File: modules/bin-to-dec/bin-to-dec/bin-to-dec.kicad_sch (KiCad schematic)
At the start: 1 part, among them J1 Conn_02x26_Odd_Even

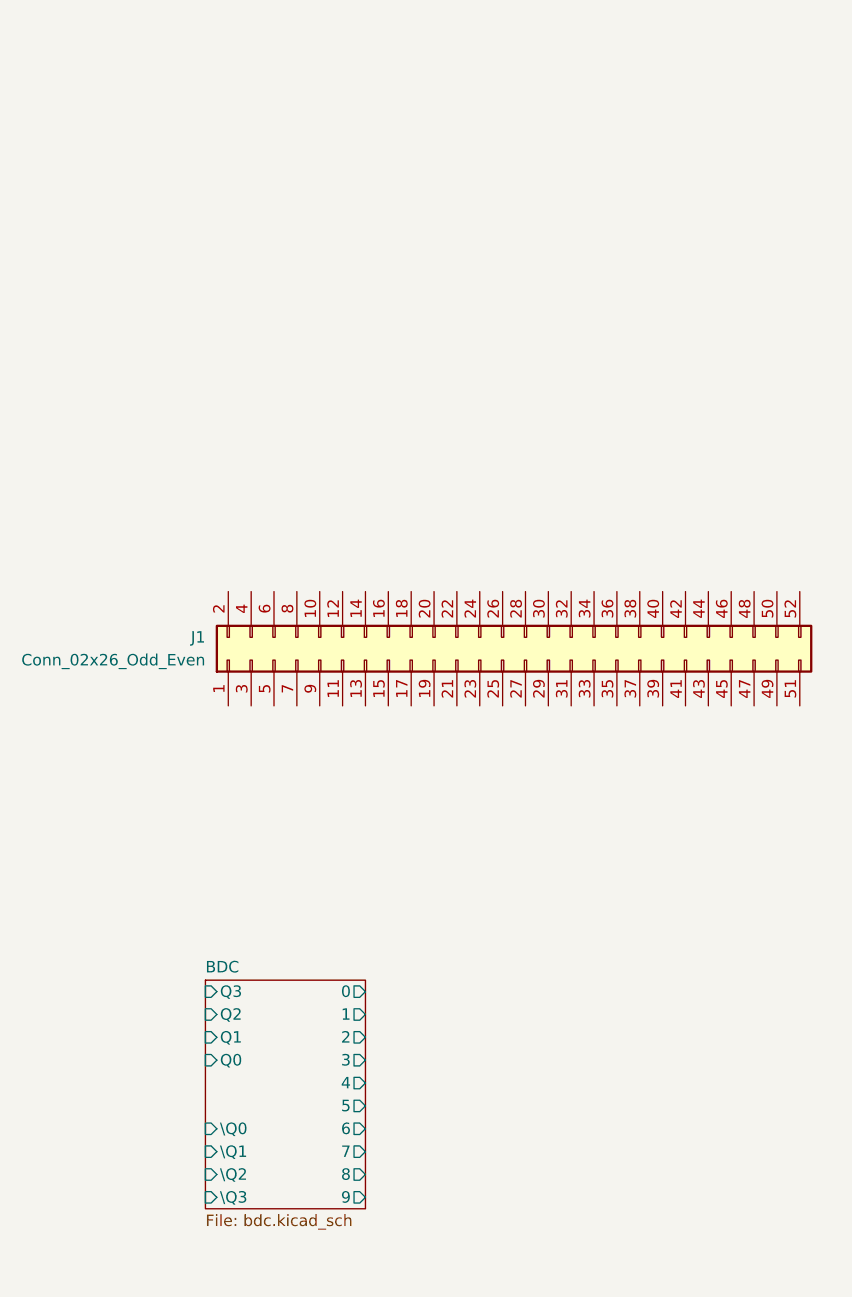
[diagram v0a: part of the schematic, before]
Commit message: routed on bdc
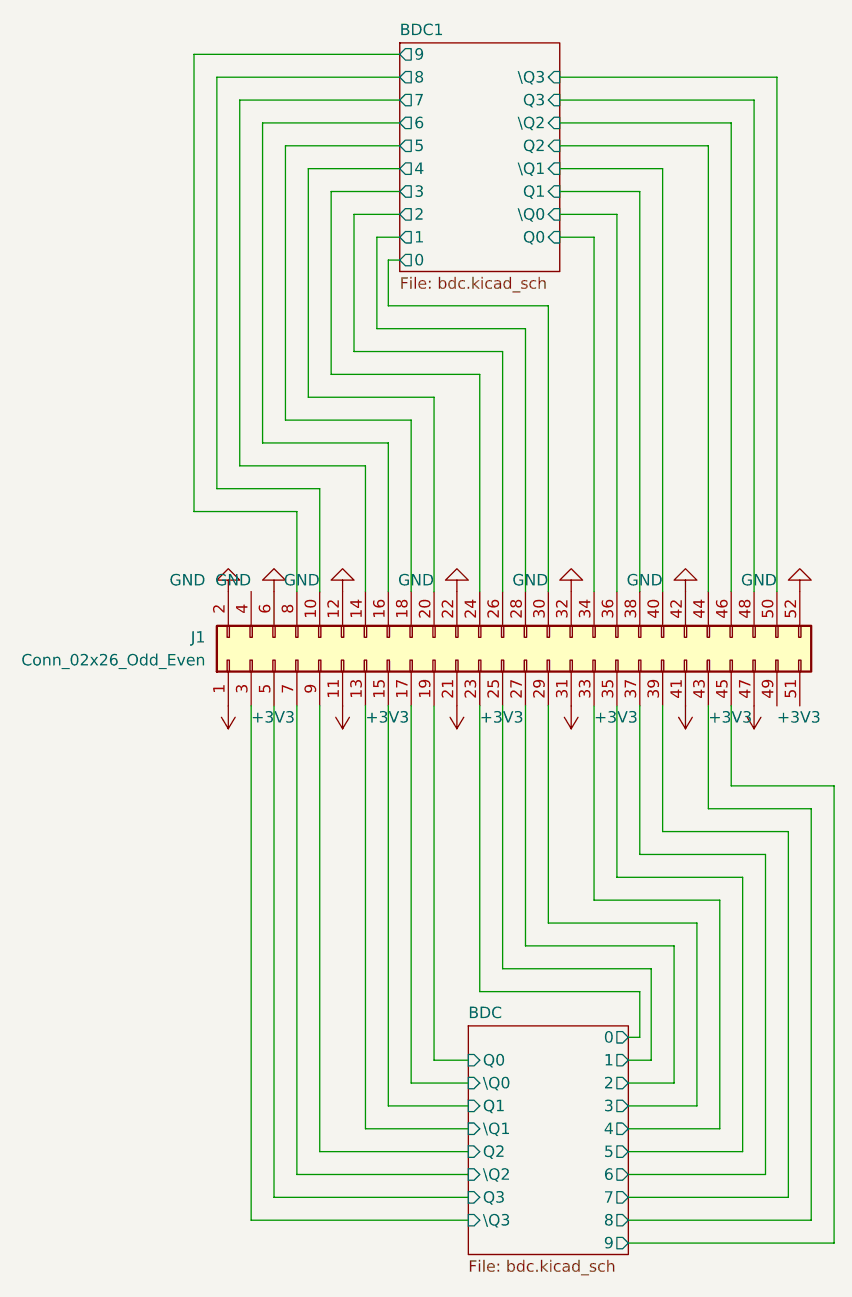
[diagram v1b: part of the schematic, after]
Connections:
- net BDC/0: now also J1.23 (Pin_23)
- net BDC/1: now also J1.25 (Pin_25)
- net BDC/2: now also J1.27 (Pin_27)
- net BDC/3: now also J1.29 (Pin_29)
- net BDC/4: now also J1.33 (Pin_33)
- net BDC/5: now also J1.35 (Pin_35)
- net BDC/6: now also J1.37 (Pin_37)
- net BDC/7: now also J1.39 (Pin_39)
- net BDC/8: now also J1.43 (Pin_43)
- net BDC/9: now also J1.45 (Pin_45)
- net BDC/Q0: now also J1.19 (Pin_19)
- net BDC/Q1: now also J1.15 (Pin_15)
- net BDC/Q2: now also J1.9 (Pin_9)
- net BDC/Q3: now also J1.5 (Pin_5)
- net BDC/\Q0: now also J1.17 (Pin_17)
- net BDC/\Q1: now also J1.13 (Pin_13)
- net BDC/\Q2: now also J1.7 (Pin_7)
- net BDC/\Q3: now also J1.3 (Pin_3)
- net +3V3: now reaches J1.1 (Pin_1)
- net +3V3: now also J1.11 (Pin_11), J1.21 (Pin_21), J1.31 (Pin_31), J1.41 (Pin_41), J1.47 (Pin_47)
- net BDC1/8: now reaches J1.10 (Pin_10)
- net GND: now reaches J1.12 (Pin_12)
- net GND: now also J1.2 (Pin_2), J1.22 (Pin_22), J1.32 (Pin_32), J1.42 (Pin_42), J1.52 (Pin_52), J1.6 (Pin_6)
- net BDC1/7: now reaches J1.14 (Pin_14)
- net BDC1/6: now reaches J1.16 (Pin_16)
- net BDC1/5: now reaches J1.18 (Pin_18)
- net BDC1/4: now reaches J1.20 (Pin_20)
- net BDC1/3: now reaches J1.24 (Pin_24)
- net BDC1/2: now reaches J1.26 (Pin_26)
- net BDC1/1: now reaches J1.28 (Pin_28)
- net BDC1/0: now reaches J1.30 (Pin_30)
- net BDC1/Q0: now reaches J1.34 (Pin_34)
- net BDC1/\Q0: now reaches J1.36 (Pin_36)
- net BDC1/Q1: now reaches J1.38 (Pin_38)
- net BDC1/\Q1: now reaches J1.40 (Pin_40)
- net BDC1/Q2: now reaches J1.44 (Pin_44)
- net BDC1/\Q2: now reaches J1.46 (Pin_46)
- net BDC1/Q3: now reaches J1.48 (Pin_48)
- net BDC1/\Q3: now reaches J1.50 (Pin_50)
- net BDC1/9: now reaches J1.8 (Pin_8)
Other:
- added sheet BDC1 (bdc.kicad_sch)

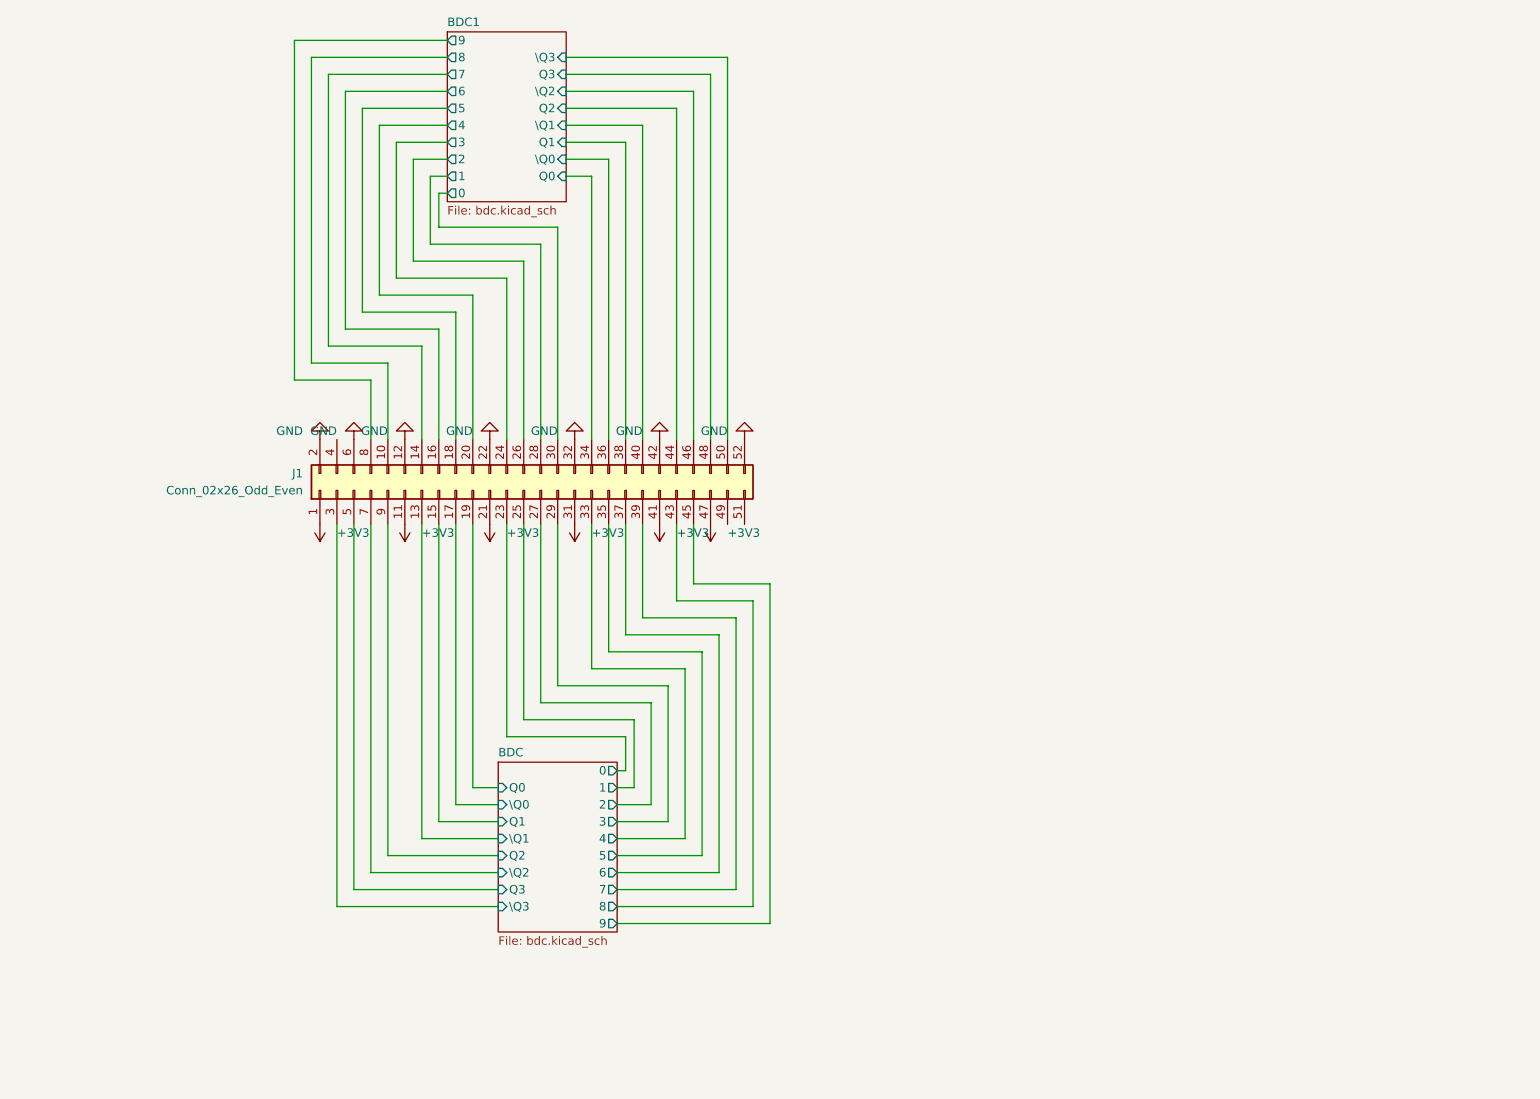
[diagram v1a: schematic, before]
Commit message: went from routed bin-to-dec to gate only
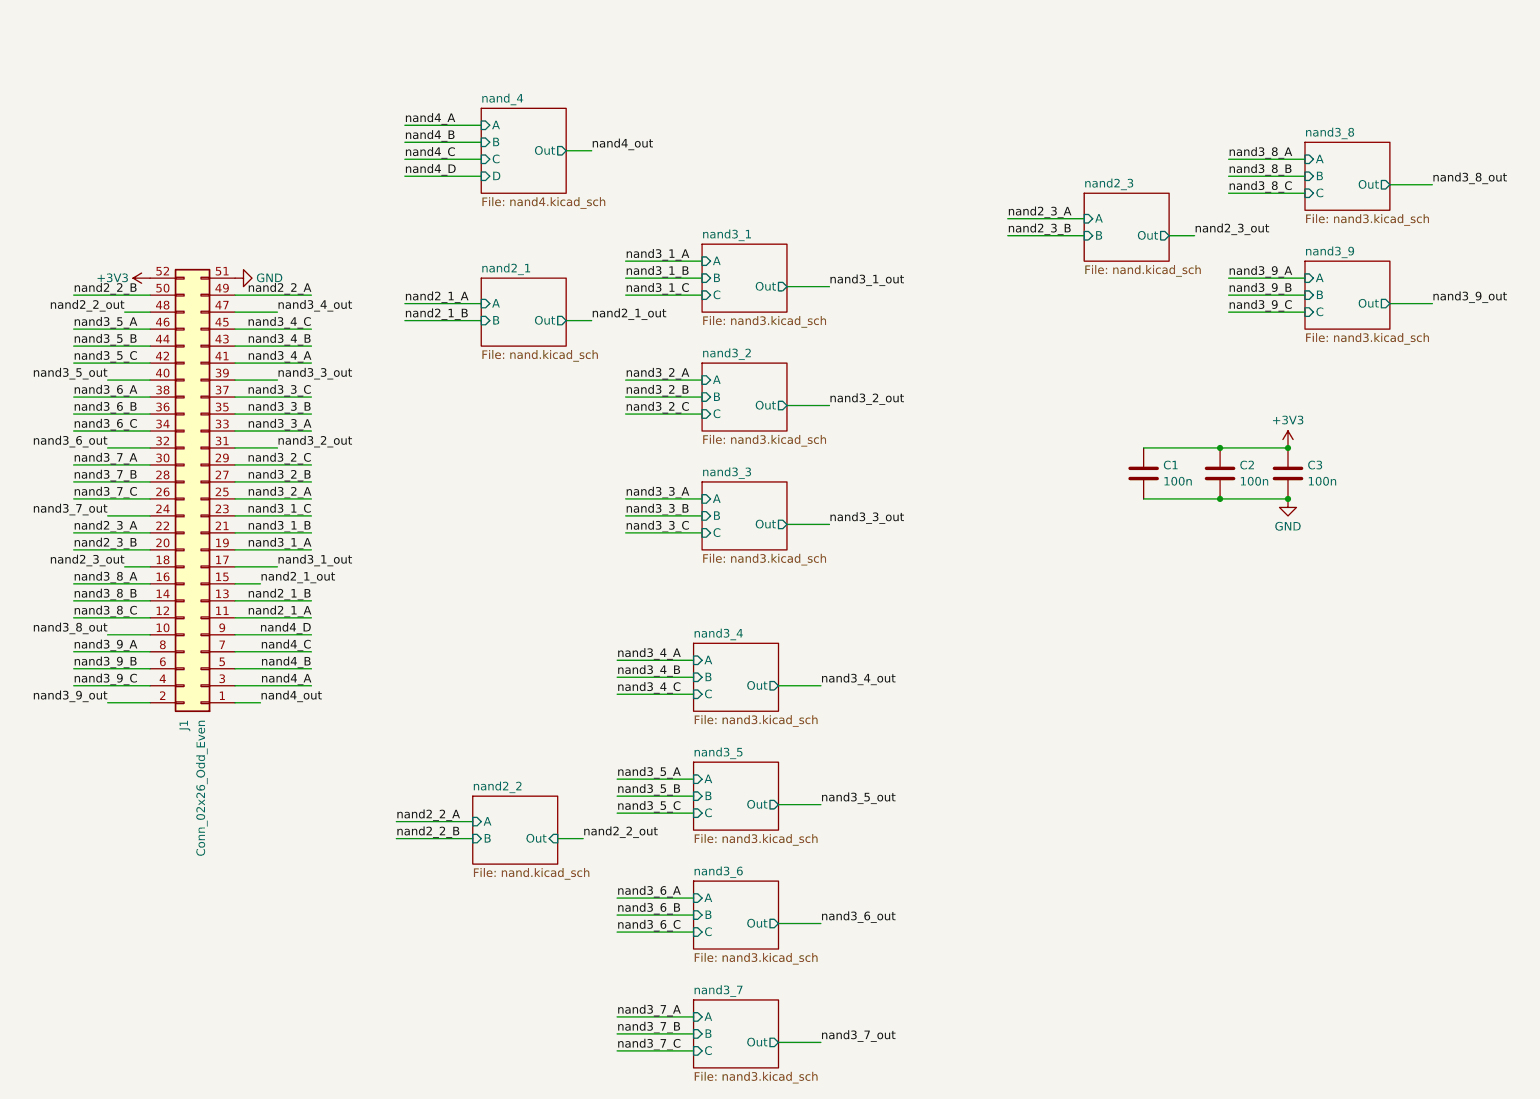
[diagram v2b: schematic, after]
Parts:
- added C1, C2, C3: 100n, Capacitor_SMD:C_0603_1608Metric, symbol Device:C
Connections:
- net +3V3: now also J1.52 (Pin_52), C1.1, C2.1, C3.1; no longer J1.1 (Pin_1), J1.11 (Pin_11), J1.21 (Pin_21), J1.31 (Pin_31), J1.41 (Pin_41), J1.47 (Pin_47)
- net GND: now also J1.51 (Pin_51), C1.2, C2.2, C3.2; no longer J1.12 (Pin_12), J1.2 (Pin_2), J1.22 (Pin_22), J1.32 (Pin_32), J1.42 (Pin_42), J1.52 (Pin_52), J1.6 (Pin_6)
- net nand3_9_C: now reaches J1.4 (Pin_4)
- net nand2_2_A: now reaches J1.49 (Pin_49)
- net BDC/0 renamed nand3_1_C
- net BDC/1 renamed nand3_2_A
- net BDC/2 renamed nand3_2_B
- net BDC/3 renamed nand3_2_C
- net BDC/4 renamed nand3_3_A
- net BDC/5 renamed nand3_3_B
- net BDC/6 renamed nand3_3_C
- net BDC/7 renamed nand3_3_out
- net BDC/8 renamed nand3_4_B
- net BDC/9 renamed nand3_4_C
- net BDC/Q0 renamed nand3_1_A
- net BDC/Q1 renamed nand2_1_out
- net BDC/Q2 renamed nand4_D
- net BDC/Q3 renamed nand4_B
- net BDC/\Q0 renamed nand3_1_out
- net BDC/\Q1 renamed nand2_1_B
- net BDC/\Q2 renamed nand4_C
- net BDC/\Q3 renamed nand4_A
- net BDC1/0 renamed nand3_7_A
- net BDC1/1 renamed nand3_7_B
- net BDC1/2 renamed nand3_7_C
- net BDC1/3 renamed nand3_7_out
- net BDC1/4 renamed nand2_3_B
- net BDC1/5 renamed nand2_3_out
- net BDC1/6 renamed nand3_8_A
- net BDC1/7 renamed nand3_8_B
- net BDC1/8 renamed nand3_8_out
- net BDC1/9 renamed nand3_9_A
- net BDC1/Q0 renamed nand3_6_C
- net BDC1/Q1 renamed nand3_6_A
- net BDC1/Q2 renamed nand3_5_B
- net BDC1/Q3 renamed nand2_2_out
- net BDC1/\Q0 renamed nand3_6_B
- net BDC1/\Q1 renamed nand3_5_out
- net BDC1/\Q2 renamed nand3_5_A
- net BDC1/\Q3 renamed nand2_2_B
- new net nand2_1_A: J1.11 (Pin_11)
- new net nand2_3_A: J1.22 (Pin_22)
- new net nand3_1_B: J1.21 (Pin_21)
- new net nand3_2_out: J1.31 (Pin_31)
- new net nand3_4_A: J1.41 (Pin_41)
- new net nand3_4_out: J1.47 (Pin_47)
- new net nand3_5_C: J1.42 (Pin_42)
- new net nand3_6_out: J1.32 (Pin_32)
- new net nand3_8_C: J1.12 (Pin_12)
- new net nand3_9_B: J1.6 (Pin_6)
- new net nand3_9_out: J1.2 (Pin_2)
- new net nand4_out: J1.1 (Pin_1)
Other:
- removed sheet BDC
- removed sheet BDC1
- added sheet nand2_1 (nand.kicad_sch)
- added sheet nand2_2 (nand.kicad_sch)
- added sheet nand2_3 (nand.kicad_sch)
- added sheet nand3_1 (nand3.kicad_sch)
- added sheet nand3_2 (nand3.kicad_sch)
- added sheet nand3_3 (nand3.kicad_sch)
- added sheet nand3_4 (nand3.kicad_sch)
- added sheet nand3_5 (nand3.kicad_sch)
- added sheet nand3_6 (nand3.kicad_sch)
- added sheet nand3_7 (nand3.kicad_sch)
- added sheet nand3_8 (nand3.kicad_sch)
- added sheet nand3_9 (nand3.kicad_sch)
- added sheet nand_4 (nand4.kicad_sch)
- moved on the sheet: J1
